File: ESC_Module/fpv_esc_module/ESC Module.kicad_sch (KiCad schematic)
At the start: 53 parts

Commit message: Fixed root started working on MCU
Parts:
- added C101, C102, C103, C104: 22uF, Capacitor_SMD:C_0805_2012Metric, symbol Device:C
- added D101, D102, D103, D104, D105, D106, D107, D108, D109, D110, D111, D112: 15V, Diode_SMD:D_0402_1005Metric, symbol Device:D_Zener
- added R113, R114, R115, R122, R123, R124: 10K, Resistor_SMD:R_0402_1005Metric, symbol Device:R
- added R116, R117, R118, R119, R120, R121: 1M, Resistor_SMD:R_0402_1005Metric, symbol Device:R
- R101, R102, R103, R104, R105, R106, R107, R108, R109, R110, R111, R112: value 10 -> 22; manf# ERJ-2RKF10R0X -> (none)
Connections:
- net +3V3: now also C103.1, C104.1
- net ESC1/HO1: now also R105.1; no longer R103.1
- net ESC1/HO2: now also R103.1; no longer R102.1
- net ESC1/HO3: now also R101.1; no longer R105.1
- net ESC1/LO1: now also R104.1; no longer R101.1
- net ESC1/LO2: now also R102.1; no longer R104.1
- net ESC1/VS1: now also D101.2 (A), R119.2
- net ESC1/VS2: now also D108.2 (A), R120.2
- net ESC1/VS3: now also D109.2 (A), R121.2
- net ESC2/VS1: now also D110.2 (A), R116.2
- net ESC2/VS2: now also D111.2 (A), R117.2
- net ESC2/VS3: now also D112.2 (A), R118.2
- net GND: now also C101.2, C102.2, C103.2, C104.2, D102.2 (A), D103.2 (A), D104.2 (A), D105.2 (A), D106.2 (A), D107.2 (A), R113.2, R114.2, R115.2, R122.2, R123.2, R124.2
- net VDD: now also C101.1, C102.1
- net at U5.1: now also R105.2, D101.1 (K), R119.1; no longer R103.2
- net at U9.1: now also R101.2, D109.1 (K), R121.1; no longer R105.2
- net at R102.2: now also U8.1, D103.1 (K), R114.1; no longer U7.1
- net at R109.2, U13.1: now also D111.1 (K), R117.1
- net at R112.2, U16.1: now also D107.1 (K), R124.1
- net at R108.2, U12.1: now also D105.1 (K), R122.1
- net at U6.1: now also R104.2, D102.1 (K), R113.1; no longer R101.2
- net at R107.2, U11.1: now also D110.1 (K), R116.1
- net at R111.2, U15.1: now also D112.1 (K), R118.1
- net at R106.2, U10.1: now also D104.1 (K), R115.1
- net at R110.2, U14.1: now also D106.1 (K), R123.1
- new net: D108.1 (K), R103.2, R120.1, U7.1
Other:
- note added: "BUK7V4R2-40H"
- moved on the sheet: R106, R107, R108, R109, R110, R111, R112, U10, U101, U102, U103, U104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

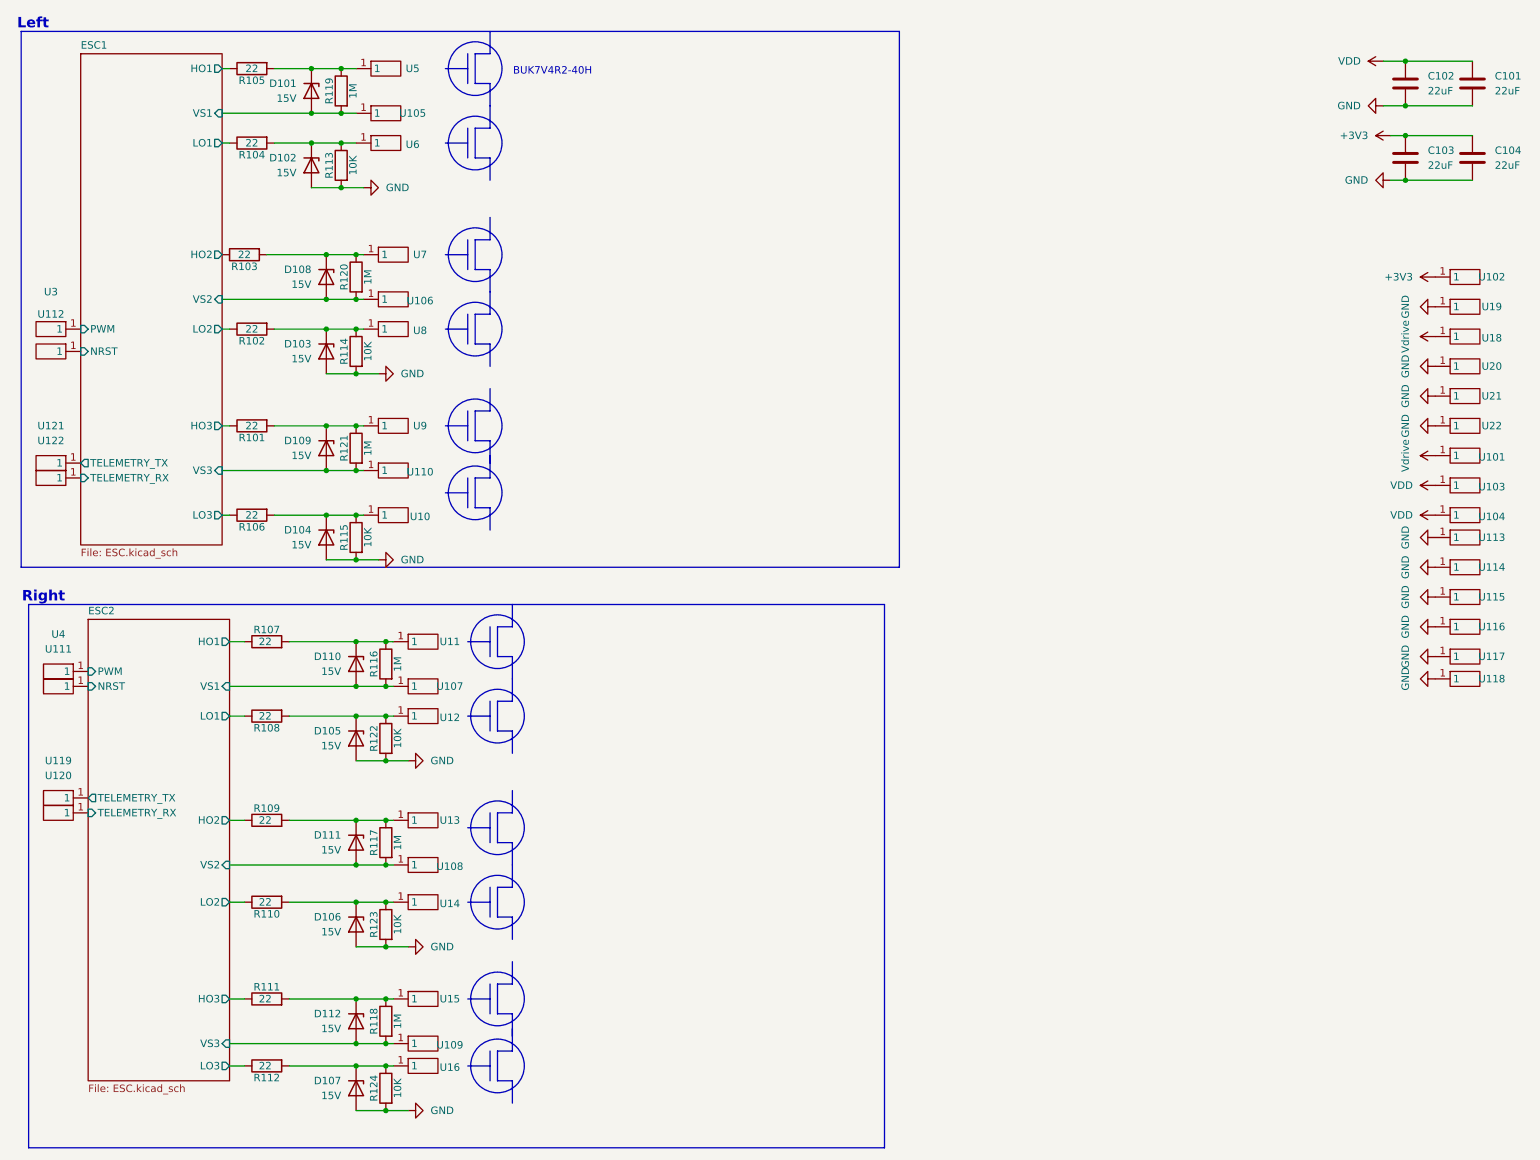
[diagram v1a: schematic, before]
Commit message: Schematic changes made
Made changes to the schematic just starting routing
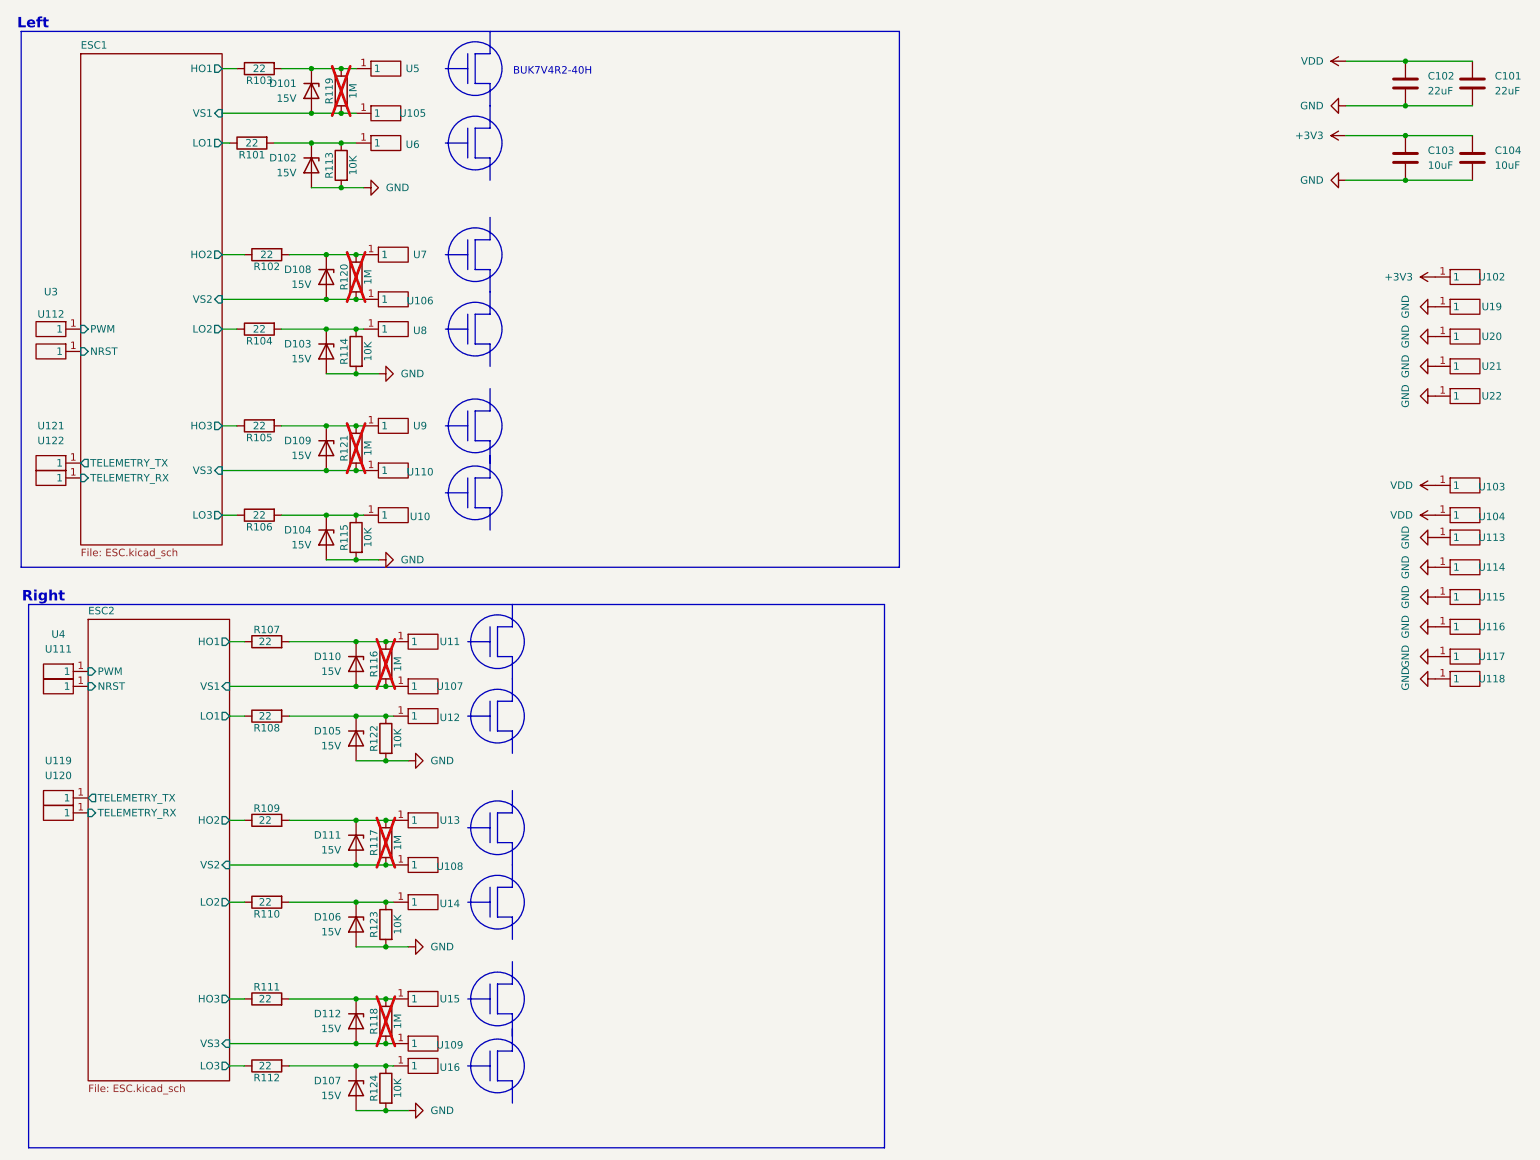
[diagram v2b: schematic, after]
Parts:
- removed U101, U18: ~, Castltated_hole:Castlated_Hole, symbol Castilated_Hole:Castilated_Hole
- C103, C104: value 22uF -> 10uF; footprint Capacitor_SMD:C_0805_2012Metric -> Capacitor_SMD:C_0402_1005Metric
- R116, R117, R118, R119, R120, R121: now not fitted
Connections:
- net ESC1/HO1: now also R103.1; no longer R105.1
- net ESC1/HO2: now also R102.1; no longer R103.1
- net ESC1/HO3: now also R105.1; no longer R101.1
- net ESC1/LO1: now also R101.1; no longer R104.1
- net ESC1/LO2: now also R104.1; no longer R102.1
- net at D101.1 (K), R119.1, U5.1: now also R103.2; no longer R105.2
- net at D102.1 (K), R113.1, U6.1: now also R101.2; no longer R104.2
- net at D103.1 (K), R114.1, U8.1: now also R104.2; no longer R102.2
- net at D108.1 (K), R120.1, U7.1: now also R102.2; no longer R103.2
- net at D109.1 (K), R121.1, U9.1: now also R105.2; no longer R101.2
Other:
- moved on the sheet: R101, R102, R103, R104, R105, R106, U20, U21, U22
